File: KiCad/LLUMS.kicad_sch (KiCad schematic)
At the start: 45 parts, among them Q1 AO3400A, Q2 AO3400A, Q3 AO3400A, Q4 AO3400A, Q5 AO3400A, Q6 AO3400A, Q7 AO3400A, Q8 AO3400A, U9 RPR-0521RS

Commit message: Huellass
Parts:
- C16: footprint (none) -> Capacitor_SMD:C_0805_2012Metric
- F1, F2, F3, F4, F5, F6, F7, F8: footprint (none) -> Fuse:Fuse_0805_2012Metric
- R1, R10, R15, R16, R17, R18, R19, R2, R20, R3, R4, R5, R6, R7, R8, R9, pull_INT1, pull_SCL2, pull_SDA2: footprint (none) -> Resistor_SMD:R_0805_2012Metric
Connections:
- net Vbat renamed VBAT
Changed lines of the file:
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@@
 		)
 	)
-	(global_label "Vbat"
+	(global_label "VBAT"
+		(shape input)
+		(at 121.92 128.27 90)
+		(fields_autoplaced yes)
+		(effects
+			(font
+				(size 1.27 1.27)
+			)
+			(justify left)
+		)
+		(property "Intersheetrefs" "${INTERSHEET_REFS}"
+			(at 121.92 120.87 90)
+			(effects
+				(font
+					(size 1.27 1.27)
+				)
+				(justify left)
+				(hide yes)
+			)
+		)
+	)
+	(global_label "VBAT"
 		(shape input)
 		(at 74.93 137.16 90)
@@
 		)
 		(property "Intersheetrefs" "${INTERSHEET_REFS}"
-			(at 74.93 130.0625 90)
+			(at 74.93 129.76 90)
 			(effects
 				(font
@@
 		)
 	)
+	(global_label "VBAT"
+		(shape input)
+		(at 39.37 41.91 90)
+		(fields_autoplaced yes)
+		(effects
+			(font
+				(size 1.27 1.27)
+			)
+			(justify left)
+		)
+		(property "Intersheetrefs" "${INTERSHEET_REFS}"
+			(at 39.37 34.51 90)
+			(effects
+				(font
+					(size 1.27 1.27)
+				)
+				(justify left)
+				(hide yes)
+			)
+		)
+	)
 	(global_label "TURN_LEFT_CTRL"
 		(shape input)
@@
 		)
 	)
-	(global_label "Vbat"
+	(global_label "VBAT"
 		(shape input)
-		(at 39.37 138.43 90)
+		(at 161.29 41.91 90)
 		(fields_autoplaced yes)
 		(effects
@@
 		)
 		(property "Intersheetrefs" "${INTERSHEET_REFS}"
-			(at 39.37 131.3325 90)
+			(at 161.29 34.51 90)
 			(effects
 				(font
@@
 		)
 	)
-	(global_label "Vbat"
+	(global_label "VBAT"
 		(shape input)
-		(at 161.29 41.91 90)
+		(at 162.56 129.54 90)
 		(fields_autoplaced yes)
 		(effects
@@
 		)
 		(property "Intersheetrefs" "${INTERSHEET_REFS}"
-			(at 161.29 34.8125 90)
+			(at 162.56 122.14 90)
 			(effects
 				(font
@@
 		)
 	)
-	(global_label "VCC"
+	(global_label "VBAT"
 		(shape input)
-		(at 248.92 46.99 90)
+		(at 39.37 138.43 90)
 		(fields_autoplaced yes)
 		(effects
@@
 		)
 		(property "Intersheetrefs" "${INTERSHEET_REFS}"
-			(at 248.92 40.3762 90)
+			(at 39.37 131.03 90)
 			(effects
 				(font
@@
 		)
 	)
-	(global_label "Vbat"
+	(global_label "VBAT"
 		(shape input)
-		(at 119.38 40.64 90)
+		(at 74.93 41.91 90)
 		(fields_autoplaced yes)
 		(effects
@@
 		)
 		(property "Intersheetrefs" "${INTERSHEET_REFS}"
-			(at 119.38 33.5425 90)
+			(at 74.93 34.51 90)
 			(effects
 				(font
@@
 		)
 	)
-	(global_label "SCL"
+	(global_label "VCC"
 		(shape input)
-		(at 212.09 67.31 180)
+		(at 248.92 46.99 90)
 		(fields_autoplaced yes)
 		(effects
@@
 				(size 1.27 1.27)
 			)
-			(justify right)
+			(justify left)
 		)
 		(property "Intersheetrefs" "${INTERSHEET_REFS}"
-			(at 205.5972 67.31 0)
+			(at 248.92 40.3762 90)
 			(effects
 				(font
 					(size 1.27 1.27)
 				)
-				(justify right)
+				(justify left)
 				(hide yes)
 			)
 		)
 	)
-	(global_label "Vbat"
+	(global_label "SCL"
 		(shape input)
-		(at 39.37 41.91 90)
+		(at 212.09 67.31 180)
 		(fields_autoplaced yes)
 		(effects
@@
 				(size 1.27 1.27)
 			)
-			(justify left)
+			(justify right)
 		)
 		(property "Intersheetrefs" "${INTERSHEET_REFS}"
-			(at 39.37 34.8125 90)
+			(at 205.5972 67.31 0)
 			(effects
 				(font
 					(size 1.27 1.27)
 				)
-				(justify left)
+				(justify right)
 				(hide yes)
 			)
@@
 		)
 	)
-	(global_label "Vbat"
-		(shape input)
-		(at 74.93 41.91 90)
-		(fields_autoplaced yes)
-		(effects
-			(font
-				(size 1.27 1.27)
-			)
-			(justify left)
-		)
-		(property "Intersheetrefs" "${INTERSHEET_REFS}"
-			(at 74.93 34.8125 90)
-			(effects
-				(font
-					(size 1.27 1.27)
-				)
-				(justify left)
-				(hide yes)
-			)
-		)
-	)
-	(global_label "Vbat"
+	(global_label "VBAT"
 		(shape input)
-		(at 121.92 128.27 90)
-		(fields_autoplaced yes)
-		(effects
-			(font
-				(size 1.27 1.27)
-			)
-			(justify left)
-		)
-		(property "Intersheetrefs" "${INTERSHEET_REFS}"
-			(at 121.92 121.1725 90)
-			(effects
-				(font
-					(size 1.27 1.27)
-				)
-				(justify left)
-				(hide yes)
-			)
-		)
-	)
-	(global_label "Vbat"
-		(shape input)
-		(at 162.56 129.54 90)
+		(at 119.38 40.64 90)
 		(fields_autoplaced yes)
 		(effects
@@
 		)
 		(property "Intersheetrefs" "${INTERSHEET_REFS}"
-			(at 162.56 122.4425 90)
+			(at 119.38 33.24 90)
 			(effects
 				(font
@@
 			)
 		)
-		(property "Footprint" ""
+		(property "Footprint" "Fuse:Fuse_0805_2012Metric"
 			(at 121.158 46.99 90)
 			(effects
@@
 			)
 		)
-		(property "Footprint" ""
+		(property "Footprint" "Resistor_SMD:R_0805_2012Metric"
 			(at 26.416 65.024 90)
 			(effects
@@
 			)
 		)
-		(property "Footprint" ""
+		(property "Footprint" "Resistor_SMD:R_0805_2012Metric"
 			(at 26.416 77.724 90)
 			(effects
@@
 			)
 		)
-		(property "Footprint" ""
+		(property "Footprint" "Fuse:Fuse_0805_2012Metric"
 			(at 76.708 143.51 90)
 			(effects
@@
 			)
 		)
-		(property "Footprint" ""
+		(property "Footprint" "Fuse:Fuse_0805_2012Metric"
 			(at 41.148 144.78 90)
 			(effects
@@
 			)
 		)
-		(property "Footprint" ""
+		(property "Footprint" "Resistor_SMD:R_0805_2012Metric"
 			(at 61.976 65.024 90)
 			(effects
@@
 			)
 		)
-		(property "Footprint" ""
+		(property "Footprint" "Resistor_SMD:R_0805_2012Metric"
 			(at 224.536 52.324 90)
 			(effects
@@
 			)
 		)
-		(property "Footprint" ""
+		(property "Footprint" "Fuse:Fuse_0805_2012Metric"
 			(at 76.708 48.26 90)
 			(effects
@@
 			)
 		)
-		(property "Footprint" ""
+		(property "Footprint" "Resistor_SMD:R_0805_2012Metric"
 			(at 228.346 52.324 90)
 			(effects
@@
 			)
 		)
-		(property "Footprint" ""
+		(property "Footprint" "Resistor_SMD:R_0805_2012Metric"
 			(at 108.966 63.754 90)
 			(effects
@@
 			)
 		)
-		(property "Footprint" ""
+		(property "Footprint" "Resistor_SMD:R_0805_2012Metric"
 			(at 150.876 165.354 90)
 			(effects
@@
 			)
 		)
-		(property "Footprint" ""
+		(property "Footprint" "Fuse:Fuse_0805_2012Metric"
 			(at 41.148 48.26 90)
 			(effects
@@
 			)
 		)
-		(property "Footprint" ""
+		(property "Footprint" "Fuse:Fuse_0805_2012Metric"
 			(at 163.068 48.26 90)
 			(effects
@@
 			)
 		)
-		(property "Footprint" ""
+		(property "Footprint" "Resistor_SMD:R_0805_2012Metric"
 			(at 61.976 77.724 90)
 			(effects
@@
 			)
 		)
-		(property "Footprint" ""
+		(property "Footprint" "Resistor_SMD:R_0805_2012Metric"
 			(at 110.236 151.384 90)
 			(effects
@@
 			)
 		)
-		(property "Footprint" ""
+		(property "Footprint" "Capacitor_SMD:C_0805_2012Metric"
 			(at 237.1852 58.42 0)
 			(effects
@@
 			)
 		)
-		(property "Footprint" ""
+		(property "Footprint" "Fuse:Fuse_0805_2012Metric"
 			(at 164.338 135.89 90)
 			(effects
@@
 			)
 		)
-		(property "Footprint" ""
+		(property "Footprint" "Fuse:Fuse_0805_2012Metric"
 			(at 123.698 134.62 90)
 			(effects
@@
 			)
 		)
-		(property "Footprint" ""
+		(property "Footprint" "Resistor_SMD:R_0805_2012Metric"
 			(at 65.786 160.274 90)
 			(effects
@@
 			)
 		)
-		(property "Footprint" ""
+		(property "Footprint" "Resistor_SMD:R_0805_2012Metric"
 			(at 65.786 172.974 90)
 			(effects
@@
 			)
 		)
-		(property "Footprint" ""
+		(property "Footprint" "Resistor_SMD:R_0805_2012Metric"
 			(at 150.876 152.654 90)
 			(effects
@@
 			)
 		)
-		(property "Footprint" ""
+		(property "Footprint" "Resistor_SMD:R_0805_2012Metric"
 			(at 30.226 174.244 90)
 			(effects
@@
 			)
 		)
-		(property "Footprint" ""
+		(property "Footprint" "Resistor_SMD:R_0805_2012Metric"
 			(at 220.726 59.944 90)
 			(effects
@@
 			)
 		)
-		(property "Footprint" ""
+		(property "Footprint" "Resistor_SMD:R_0805_2012Metric"
 			(at 110.236 164.084 90)
 			(effects
@@
 			)
 		)
-		(property "Footprint" ""
+		(property "Footprint" "Resistor_SMD:R_0805_2012Metric"
 			(at 30.226 161.544 90)
 			(effects
@@
 			)
 		)
-		(property "Footprint" ""
+		(property "Footprint" "Resistor_SMD:R_0805_2012Metric"
 			(at 150.876 63.754 90)
 			(effects
@@
 			)
 		)
-		(property "Footprint" ""
+		(property "Footprint" "Resistor_SMD:R_0805_2012Metric"
 			(at 150.876 76.454 90)
 			(effects
@@
 			)
 		)
-		(property "Footprint" ""
+		(property "Footprint" "Resistor_SMD:R_0805_2012Metric"
 			(at 108.966 76.454 90)
 			(effects

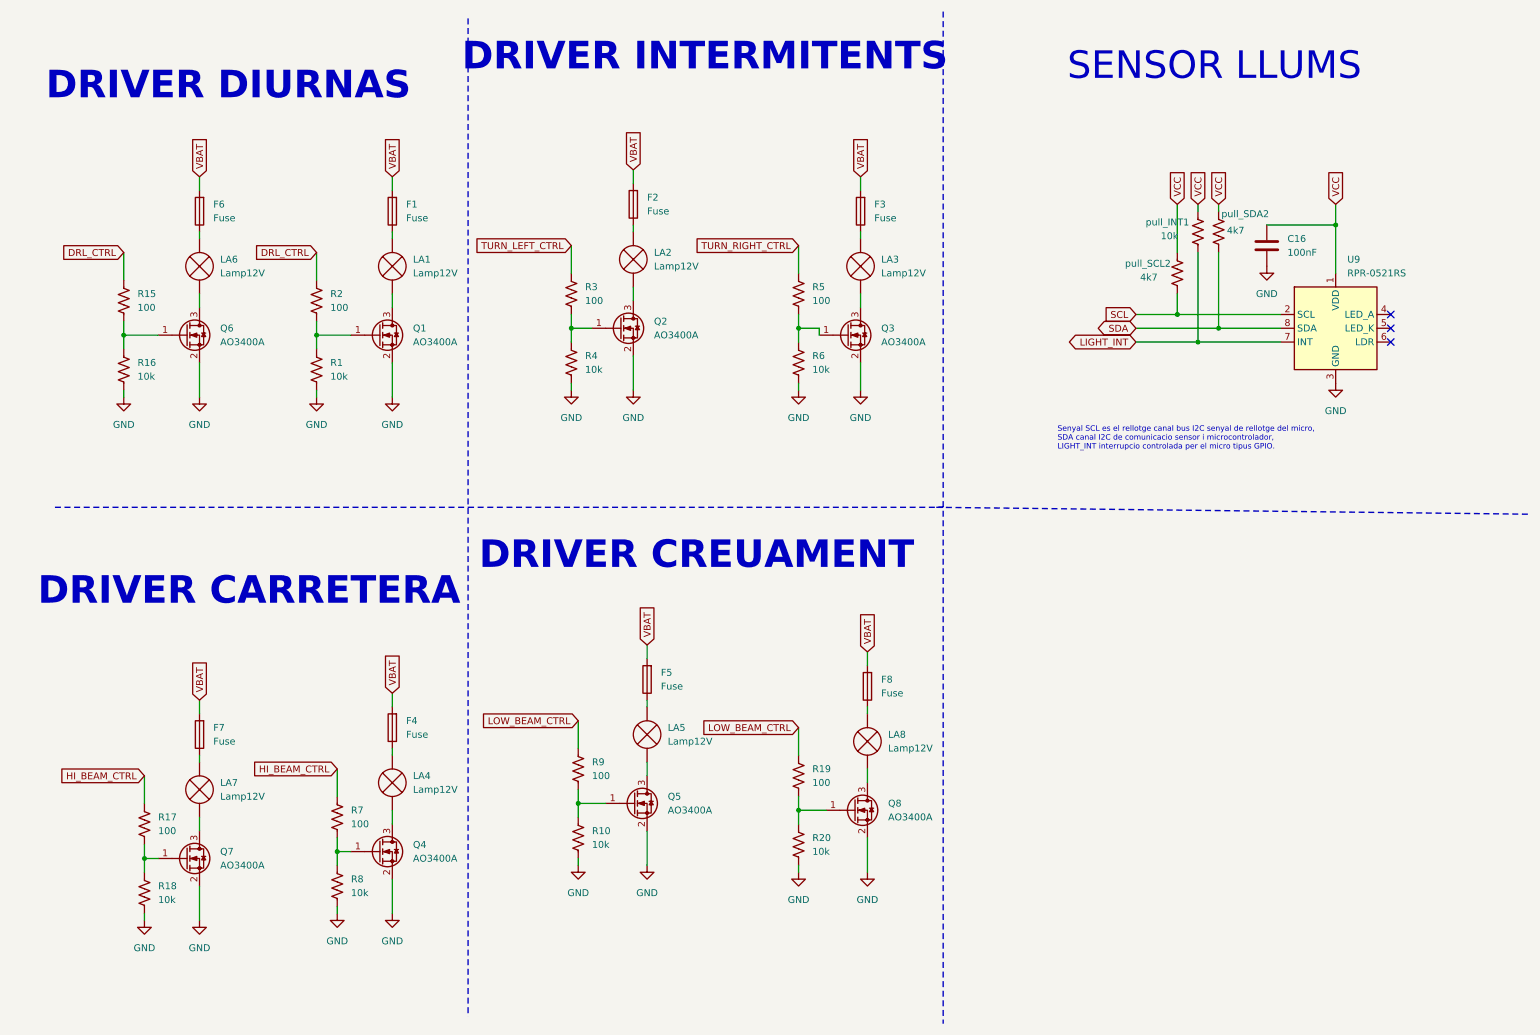
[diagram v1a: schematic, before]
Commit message: Hotfix for driver leds
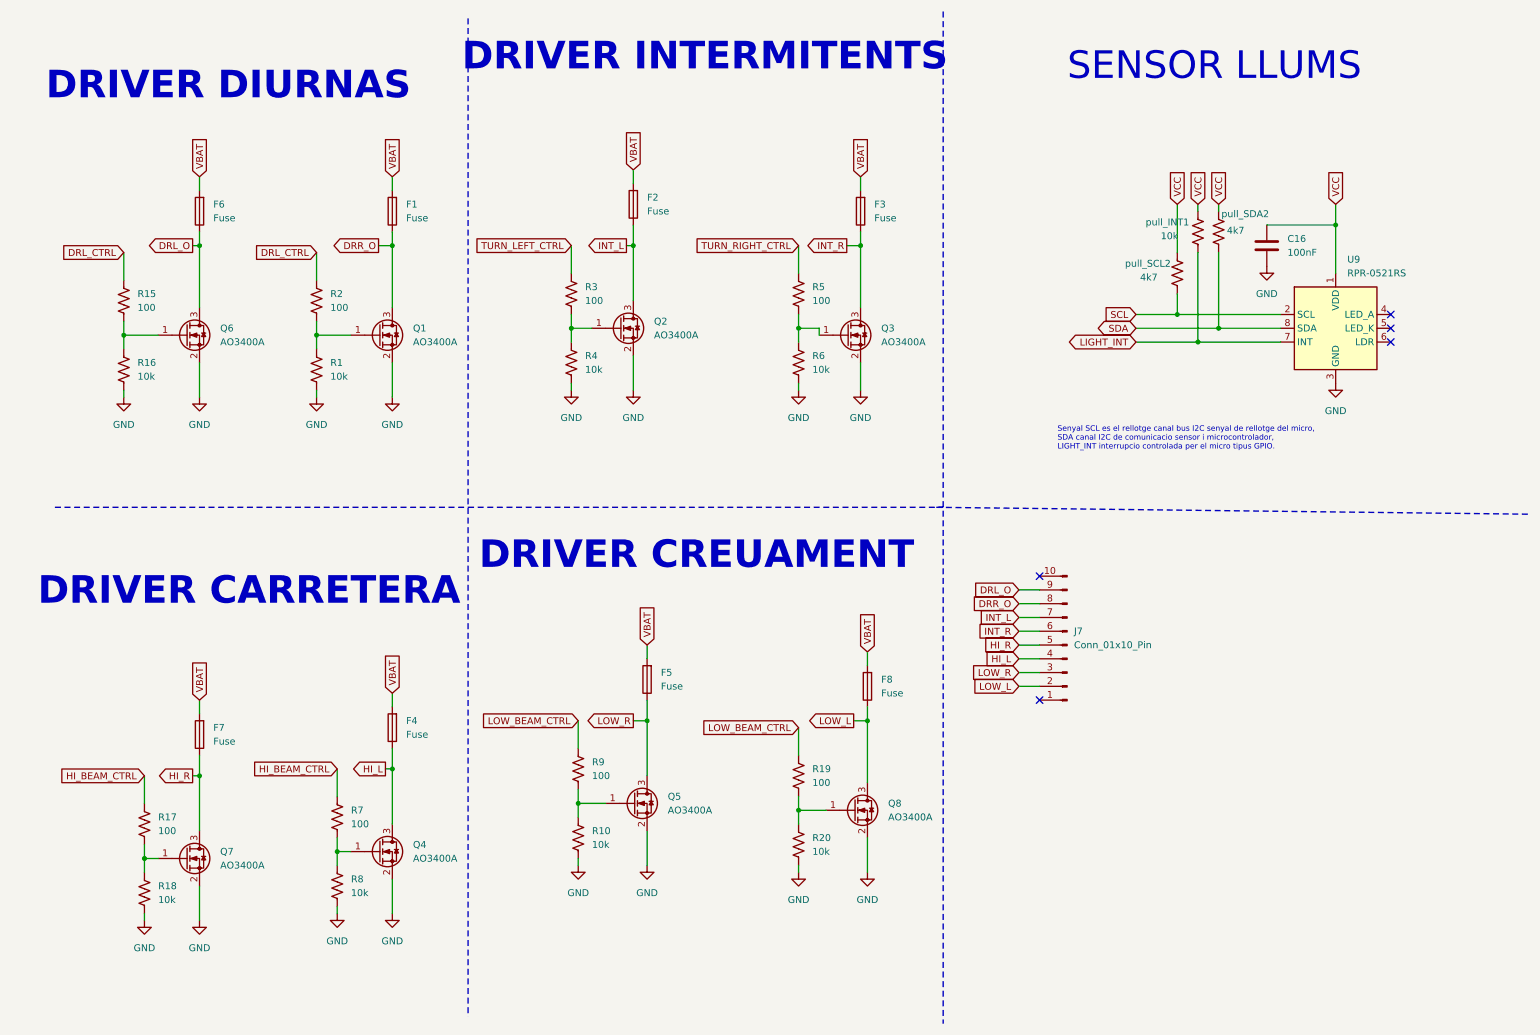
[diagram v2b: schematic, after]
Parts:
- removed LA1, LA2, LA3, LA4, LA5, LA6, LA7, LA8: Lamp12V, symbol Device:Lamp
- added J7: Conn_01x10_Pin, Connector_PinHeader_2.54mm:PinHeader_1x10_P2.54mm_Vertical, symbol Connector:Conn_01x10_Pin
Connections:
- net INT_L: now reaches F2.1
- net INT_L: now also Q2.3 (D), J7.7 (Pin_7)
- net HI_L: now reaches F4.1
- net HI_L: now also Q4.3 (D), J7.4 (Pin_4)
- net HI_R: now reaches F7.1
- net HI_R: now also Q7.3 (D), J7.5 (Pin_5)
- net INT_R: now reaches Q3.3 (D)
- net INT_R: now also F3.1, J7.6 (Pin_6)
- net LOW_R: now reaches Q5.3 (D)
- net LOW_R: now also F5.1, J7.3 (Pin_3)
- net DRR_O: now reaches F1.1
- net DRR_O: now also Q1.3 (D), J7.8 (Pin_8)
- net LOW_L: now reaches Q8.3 (D)
- net LOW_L: now also F8.1, J7.2 (Pin_2)
- net DRL_O: now reaches Q6.3 (D)
- net DRL_O: now also F6.1, J7.9 (Pin_9)
- no-connect marks 3 -> 5

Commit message: Placa
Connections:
- net HI_L: now also J7.2 (Pin_2); no longer J7.4 (Pin_4)
- net HI_R: now also J7.3 (Pin_3); no longer J7.5 (Pin_5)
- net LOW_L: now also J7.4 (Pin_4); no longer J7.2 (Pin_2)
- net LOW_R: now also J7.5 (Pin_5); no longer J7.3 (Pin_3)
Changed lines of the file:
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@@
-		)
-	)
-	(global_label "LOW_L"
-		(shape input)
-		(at 190.5 135.89 180)
-		(fields_autoplaced yes)
-		(effects
-			(font
-				(size 1.27 1.27)
-			)
-			(justify right)
-		)
-		(property "Intersheetrefs" "${INTERSHEET_REFS}"
-			(at 181.7091 135.89 0)
-			(effects
-				(font
-					(size 1.27 1.27)
-				)
-				(justify right)
-				(hide yes)
-			)
 		)
 	)
@@
 		)
 	)
+	(global_label "LOW_R"
+		(shape input)
+		(at 190.5 128.27 180)
+		(fields_autoplaced yes)
+		(effects
+			(font
+				(size 1.27 1.27)
+			)
+			(justify right)
+		)
+		(property "Intersheetrefs" "${INTERSHEET_REFS}"
+			(at 181.4672 128.27 0)
+			(effects
+				(font
+					(size 1.27 1.27)
+				)
+				(justify right)
+				(hide yes)
+			)
+		)
+	)
 	(global_label "VCC"
 		(shape input)
@@
 				)
 				(justify left)
-				(hide yes)
-			)
-		)
-	)
-	(global_label "HI_L"
-		(shape input)
-		(at 190.5 130.81 180)
-		(fields_autoplaced yes)
-		(effects
-			(font
-				(size 1.27 1.27)
-			)
-			(justify right)
-		)
-		(property "Intersheetrefs" "${INTERSHEET_REFS}"
-			(at 183.5838 130.81 0)
-			(effects
-				(font
-					(size 1.27 1.27)
-				)
-				(justify right)
 				(hide yes)
 			)
@@
 		)
 	)
-	(global_label "LOW_R"
-		(shape input)
-		(at 190.5 133.35 180)
-		(fields_autoplaced yes)
-		(effects
-			(font
-				(size 1.27 1.27)
-			)
-			(justify right)
-		)
-		(property "Intersheetrefs" "${INTERSHEET_REFS}"
-			(at 181.4672 133.35 0)
-			(effects
-				(font
-					(size 1.27 1.27)
-				)
-				(justify right)
-				(hide yes)
-			)
-		)
-	)
 	(global_label "HI_BEAM_CTRL"
 		(shape input)
@@
 		)
 	)
+	(global_label "HI_L"
+		(shape input)
+		(at 190.5 135.89 180)
+		(fields_autoplaced yes)
+		(effects
+			(font
+				(size 1.27 1.27)
+			)
+			(justify right)
+		)
+		(property "Intersheetrefs" "${INTERSHEET_REFS}"
+			(at 183.5838 135.89 0)
+			(effects
+				(font
+					(size 1.27 1.27)
+				)
+				(justify right)
+				(hide yes)
+			)
+		)
+	)
 	(global_label "DRL_O"
 		(shape output)
@@
 		)
 	)
+	(global_label "LOW_L"
+		(shape input)
+		(at 190.5 130.81 180)
+		(fields_autoplaced yes)
+		(effects
+			(font
+				(size 1.27 1.27)
+			)
+			(justify right)
+		)
+		(property "Intersheetrefs" "${INTERSHEET_REFS}"
+			(at 181.7091 130.81 0)
+			(effects
+				(font
+					(size 1.27 1.27)
+				)
+				(justify right)
+				(hide yes)
+			)
+		)
+	)
+	(global_label "SCL"
+		(shape input)
+		(at 212.09 67.31 180)
+		(fields_autoplaced yes)
+		(effects
+			(font
+				(size 1.27 1.27)
+			)
+			(justify right)
+		)
+		(property "Intersheetrefs" "${INTERSHEET_REFS}"
+			(at 205.5972 67.31 0)
+			(effects
+				(font
+					(size 1.27 1.27)
+				)
+				(justify right)
+				(hide yes)
+			)
+		)
+	)
 	(global_label "HI_R"
 		(shape input)
-		(at 190.5 128.27 180)
-		(fields_autoplaced yes)
-		(effects
-			(font
-				(size 1.27 1.27)
-			)
-			(justify right)
-		)
-		(property "Intersheetrefs" "${INTERSHEET_REFS}"
-			(at 183.3419 128.27 0)
-			(effects
-				(font
-					(size 1.27 1.27)
-				)
-				(justify right)
-				(hide yes)
-			)
-		)
-	)
-	(global_label "SCL"
-		(shape input)
-		(at 212.09 67.31 180)
-		(fields_autoplaced yes)
-		(effects
-			(font
-				(size 1.27 1.27)
-			)
-			(justify right)
-		)
-		(property "Intersheetrefs" "${INTERSHEET_REFS}"
-			(at 205.5972 67.31 0)
-			(effects
-				(font
+		(at 190.5 133.35 180)
+		(fields_autoplaced yes)
+		(effects
+			(font
+				(size 1.27 1.27)
+			)
+			(justify right)
+		)
+		(property "Intersheetrefs" "${INTERSHEET_REFS}"
+			(at 183.3419 133.35 0)
+			(effects
+				(font

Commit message: a
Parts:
- removed F1, F2, F3, F4, F5, F6, F7, F8: Fuse, Fuse:Fuse_0805_2012Metric, symbol Device:Fuse
- removed J7: Conn_01x10_Pin, Connector_PinHeader_2.54mm:PinHeader_1x10_P2.54mm_Vertical, symbol Connector:Conn_01x10_Pin
- added J10, J11, J12, J13, J14, J7, J8, J9: Screw_Terminal_01x02, TerminalBlock_Phoenix:TerminalBlock_Phoenix_MKDS-1,5-2-5.08_1x02_P5.08mm_Horizontal, symbol Connector:Screw_Terminal_01x02
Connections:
- net DRL_O: now also J7.2 (Pin_2)
- net DRR_O: now also J8.2 (Pin_2)
- net HI_L: now also J12.2 (Pin_2)
- net HI_R: now also J11.2 (Pin_2)
- net INT_L: now also J9.2 (Pin_2)
- net INT_R: now also J10.2 (Pin_2)
- net LOW_L: now also J14.2 (Pin_2)
- net LOW_R: now also J13.2 (Pin_2)
- net VBAT: now also Q1.1 (G), Q2.1 (G), Q3.1 (G), Q4.1 (G), Q5.1 (G), Q6.1 (G), Q7.1 (G), Q8.1 (G), R1.1, R10.1, R15.2, R16.1, R17.2, R18.1, R19.2, R2.2, R20.1, R3.2, R4.1, R5.2, R6.1, R7.2, R8.1, R9.2, J10.1 (Pin_1), J11.1 (Pin_1), J12.1 (Pin_1), J13.1 (Pin_1), J14.1 (Pin_1), J7.1 (Pin_1), J8.1 (Pin_1), J9.1 (Pin_1)
- no-connect marks 5 -> 3

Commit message: Finished
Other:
- company: (none) -> Marcel Lleonart, Eric Ruiz, Josep Leyva
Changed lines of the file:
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@@
 		(title "LLUMS")
 		(date "2026-03-16")
+		(rev "28/04/2026")
+		(company "Marcel Lleonart, Eric Ruiz, Josep Leyva")
 	)
 	(text "DRIVER INTERMITENTS"
